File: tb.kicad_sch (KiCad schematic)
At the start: 67 parts, among them U4 JHL6340SLLSQ, U5 MX25L8006EM1I-12G, U6 SI52112-B6-GT, U7 MX25L8006EM2I-12G, Y1 ABM8G-25.000MHZ-B4Y-T, Y2 ABM8G-25.000MHZ-B4Y-T

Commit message: Run kmake loclib
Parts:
- C100, C102, C103, C105, C106, C107, C108, C109, C110, C111, C112, C99: footprint antmicro-footprints:C_0402_1005Metric -> thunderbolt-adapter-footprints:C_0402_1005Metric; symbol antmicroCapacitors0402:C_220n_0402 -> thunderbolt-adapter:C_220n_0402
- C101, C104, C115, C98: footprint antmicro-footprints:C_0402_1005Metric -> thunderbolt-adapter-footprints:C_0402_1005Metric; symbol antmicroCapacitors0402:C_100n_0402 -> thunderbolt-adapter:C_100n_0402
- C113, C114, C116, C117: footprint antmicro-footprints:C_0402_1005Metric -> thunderbolt-adapter-footprints:C_0402_1005Metric; symbol antmicroCapacitors0402:C_10p_0402 -> thunderbolt-adapter:C_10p_0402
- R50, R51, R52, R53: footprint antmicro-footprints:R_0402_1005Metric -> thunderbolt-adapter-footprints:R_0402_1005Metric; symbol antmicroResistors0402:R_3k3_0402 -> thunderbolt-adapter:R_3k3_0402
- R54, R55, R70, R71, R82: footprint antmicro-footprints:R_0402_1005Metric -> thunderbolt-adapter-footprints:R_0402_1005Metric; symbol antmicroResistors0402:R_1M_0402 -> thunderbolt-adapter:R_1M_0402
- R56, R64, R65, R66, R67, R78, R79, R80, R83, R85: footprint antmicro-footprints:R_0402_1005Metric -> thunderbolt-adapter-footprints:R_0402_1005Metric; symbol antmicroResistors0402:R_10k_0402 -> thunderbolt-adapter:R_10k_0402
- R57, R60, R72, R75, R77, R81, R84, R86, R87, R90: footprint antmicro-footprints:R_0402_1005Metric -> thunderbolt-adapter-footprints:R_0402_1005Metric; symbol antmicroResistors0402:R_100k_0402 -> thunderbolt-adapter:R_100k_0402
- R58, R59, R61, R62: footprint antmicro-footprints:R_0402_1005Metric -> thunderbolt-adapter-footprints:R_0402_1005Metric; symbol antmicroResistors0402:R_2k2_0402 -> thunderbolt-adapter:R_2k2_0402
- R63, R76: footprint antmicro-footprints:R_0402_1005Metric -> thunderbolt-adapter-footprints:R_0402_1005Metric; symbol antmicroResistors0402:R_14k_0402 -> thunderbolt-adapter:R_14k_0402
- R68, R73: footprint antmicro-footprints:R_0402_1005Metric -> thunderbolt-adapter-footprints:R_0402_1005Metric; symbol antmicroResistors0402:R_499R_0402 -> thunderbolt-adapter:R_499R_0402
- R69: footprint antmicro-footprints:R_0402_1005Metric -> thunderbolt-adapter-footprints:R_0402_1005Metric; symbol antmicroResistors0402:R_4k75_0.5%_0402 -> thunderbolt-adapter:R_4k75_0.5%_0402
- R74: footprint antmicro-footprints:R_0402_1005Metric -> thunderbolt-adapter-footprints:R_0402_1005Metric; symbol antmicroResistors0402:R_3k01_0402 -> thunderbolt-adapter:R_3k01_0402
- R88, R89: footprint antmicro-footprints:R_0402_1005Metric -> thunderbolt-adapter-footprints:R_0402_1005Metric; symbol antmicroResistors0402:R_100R_0402 -> thunderbolt-adapter:R_100R_0402
- U4: footprint antmicro-footprints:JHL6340SLLSQ -> thunderbolt-adapter-footprints:JHL6340SLLSQ; symbol antmicroInterfaceControllers:JHL6340SLLSQ -> thunderbolt-adapter:JHL6340SLLSQ
- U5: footprint antmicro-footprints:SOIC-8_3.9x4.9x1.75mm_P1.27mm -> thunderbolt-adapter-footprints:SOIC-8_3.9x4.9x1.75mm_P1.27mm; symbol antmicroMemory:MX25L8006EM1I-12G -> thunderbolt-adapter:MX25L8006EM1I-12G
- U6: footprint antmicro-footprints:TSSOP-8_3x4.4mm_P0.65mm -> thunderbolt-adapter-footprints:TSSOP-8_3x4.4mm_P0.65mm; symbol antmicroClockTimingClockGeneratorsPLLsFrequencySynthesizers:SI52112-B6-GT -> thunderbolt-adapter:SI52112-B6-GT
- U7: footprint antmicro-footprints:SOIC-8_5.3x5.3x2mm_P1.27mm -> thunderbolt-adapter-footprints:SOIC-8_5.3x5.3x2mm_P1.27mm; symbol antmicroMemory:MX25L8006EM2I-12G -> thunderbolt-adapter:MX25L8006EM2I-12G
- Y1, Y2: footprint antmicro-footprints:Oscillator_SMD_Geyer_KX-7-4Pin_3.2x2.5mm -> thunderbolt-adapter-footprints:Oscillator_SMD_Geyer_KX-7-4Pin_3.2x2.5mm; symbol antmicroCrystals:ABM8G-25.000MHZ-B4Y-T -> thunderbolt-adapter:ABM8G-25.000MHZ-B4Y-T

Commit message: Rename project to thunderbolt-gpu-adapter
Fix Amphenol 10146070-113Y0LF footprint
Add missing 3D models, update selected footprints
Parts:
- C100, C102, C103, C105, C106, C107, C108, C109, C110, C111, C112, C99: footprint thunderbolt-adapter-footprints:C_0402_1005Metric -> thunderbolt-gpu-adapter-footprints:C_0402_1005Metric; symbol thunderbolt-adapter:C_220n_0402 -> thunderbolt-gpu-adapter:C_220n_0402
- C101, C104, C115, C98: footprint thunderbolt-adapter-footprints:C_0402_1005Metric -> thunderbolt-gpu-adapter-footprints:C_0402_1005Metric; symbol thunderbolt-adapter:C_100n_0402 -> thunderbolt-gpu-adapter:C_100n_0402
- C113, C114, C116, C117: footprint thunderbolt-adapter-footprints:C_0402_1005Metric -> thunderbolt-gpu-adapter-footprints:C_0402_1005Metric; symbol thunderbolt-adapter:C_10p_0402 -> thunderbolt-gpu-adapter:C_10p_0402
- R50, R51, R52, R53: footprint thunderbolt-adapter-footprints:R_0402_1005Metric -> thunderbolt-gpu-adapter-footprints:R_0402_1005Metric; symbol thunderbolt-adapter:R_3k3_0402 -> thunderbolt-gpu-adapter:R_3k3_0402
- R54, R55, R70, R71, R82: footprint thunderbolt-adapter-footprints:R_0402_1005Metric -> thunderbolt-gpu-adapter-footprints:R_0402_1005Metric; symbol thunderbolt-adapter:R_1M_0402 -> thunderbolt-gpu-adapter:R_1M_0402
- R56, R64, R65, R66, R67, R78, R79, R80, R83, R85: footprint thunderbolt-adapter-footprints:R_0402_1005Metric -> thunderbolt-gpu-adapter-footprints:R_0402_1005Metric; symbol thunderbolt-adapter:R_10k_0402 -> thunderbolt-gpu-adapter:R_10k_0402
- R57, R60, R72, R75, R77, R81, R84, R86, R87, R90: footprint thunderbolt-adapter-footprints:R_0402_1005Metric -> thunderbolt-gpu-adapter-footprints:R_0402_1005Metric; symbol thunderbolt-adapter:R_100k_0402 -> thunderbolt-gpu-adapter:R_100k_0402
- R58, R59, R61, R62: footprint thunderbolt-adapter-footprints:R_0402_1005Metric -> thunderbolt-gpu-adapter-footprints:R_0402_1005Metric; symbol thunderbolt-adapter:R_2k2_0402 -> thunderbolt-gpu-adapter:R_2k2_0402
- R63, R76: footprint thunderbolt-adapter-footprints:R_0402_1005Metric -> thunderbolt-gpu-adapter-footprints:R_0402_1005Metric; symbol thunderbolt-adapter:R_14k_0402 -> thunderbolt-gpu-adapter:R_14k_0402
- R68, R73: footprint thunderbolt-adapter-footprints:R_0402_1005Metric -> thunderbolt-gpu-adapter-footprints:R_0402_1005Metric; symbol thunderbolt-adapter:R_499R_0402 -> thunderbolt-gpu-adapter:R_499R_0402
- R69: footprint thunderbolt-adapter-footprints:R_0402_1005Metric -> thunderbolt-gpu-adapter-footprints:R_0402_1005Metric; symbol thunderbolt-adapter:R_4k75_0.5%_0402 -> thunderbolt-gpu-adapter:R_4k75_0.5%_0402
- R74: footprint thunderbolt-adapter-footprints:R_0402_1005Metric -> thunderbolt-gpu-adapter-footprints:R_0402_1005Metric; symbol thunderbolt-adapter:R_3k01_0402 -> thunderbolt-gpu-adapter:R_3k01_0402
- R88, R89: footprint thunderbolt-adapter-footprints:R_0402_1005Metric -> thunderbolt-gpu-adapter-footprints:R_0402_1005Metric; symbol thunderbolt-adapter:R_100R_0402 -> thunderbolt-gpu-adapter:R_100R_0402
- U4: footprint thunderbolt-adapter-footprints:JHL6340SLLSQ -> thunderbolt-gpu-adapter-footprints:JHL6340SLLSQ; symbol thunderbolt-adapter:JHL6340SLLSQ -> thunderbolt-gpu-adapter:JHL6340SLLSQ
- U5: footprint thunderbolt-adapter-footprints:SOIC-8_3.9x4.9x1.75mm_P1.27mm -> thunderbolt-gpu-adapter-footprints:SOIC-8_3.9x4.9x1.75mm_P1.27mm; symbol thunderbolt-adapter:MX25L8006EM1I-12G -> thunderbolt-gpu-adapter:MX25L8006EM1I-12G
- U6: footprint thunderbolt-adapter-footprints:TSSOP-8_3x4.4mm_P0.65mm -> thunderbolt-gpu-adapter-footprints:TSSOP-8_3x4.4mm_P0.65mm; symbol thunderbolt-adapter:SI52112-B6-GT -> thunderbolt-gpu-adapter:SI52112-B6-GT
- U7: footprint thunderbolt-adapter-footprints:SOIC-8_5.3x5.3x2mm_P1.27mm -> thunderbolt-gpu-adapter-footprints:SOIC-8_5.3x5.3x2mm_P1.27mm; symbol thunderbolt-adapter:MX25L8006EM2I-12G -> thunderbolt-gpu-adapter:MX25L8006EM2I-12G
- Y1, Y2: footprint thunderbolt-adapter-footprints:Oscillator_SMD_Geyer_KX-7-4Pin_3.2x2.5mm -> thunderbolt-gpu-adapter-footprints:Oscillator_SMD_Geyer_KX-7-4Pin_3.2x2.5mm; symbol thunderbolt-adapter:ABM8G-25.000MHZ-B4Y-T -> thunderbolt-gpu-adapter:ABM8G-25.000MHZ-B4Y-T

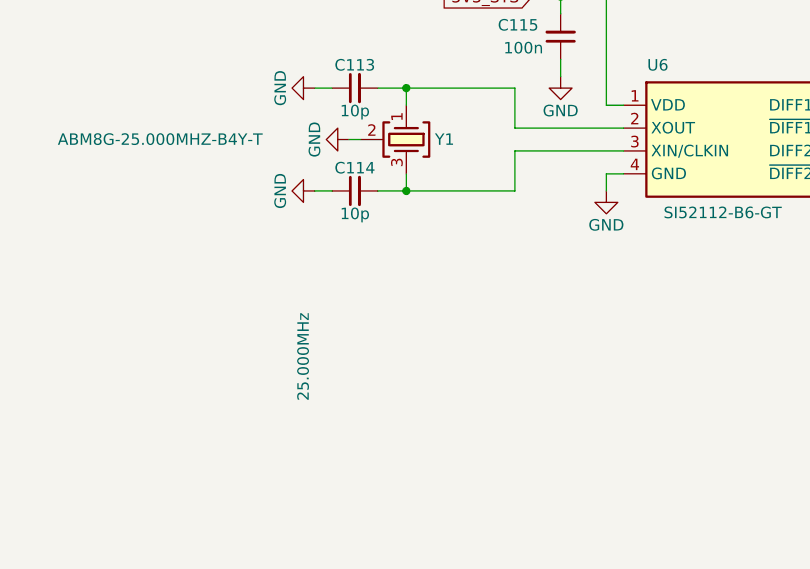
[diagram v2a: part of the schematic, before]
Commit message: Fix PCIe power switch - layout, bump revision to 1.1.2
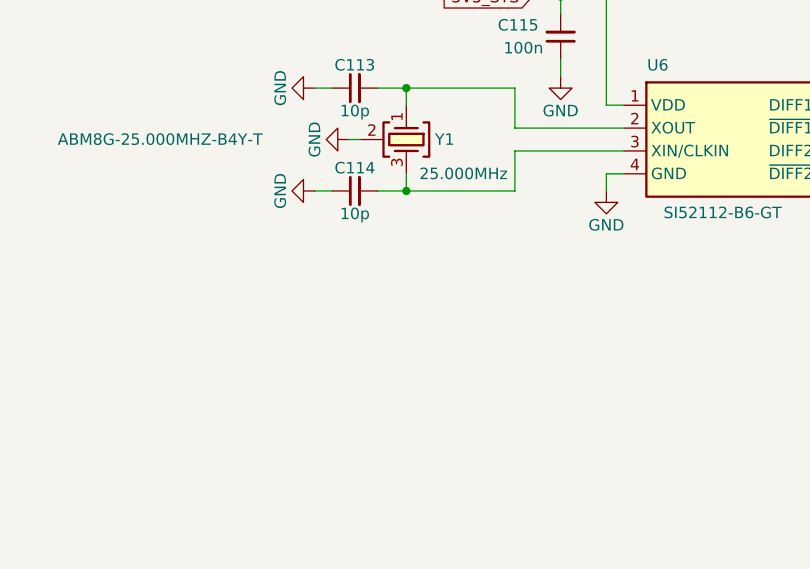
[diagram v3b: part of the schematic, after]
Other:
- company: (none) -> Antmicro Ltd
- title: Thunderbolt to PCIe bridge -> Thunderbolt GPU Adapter
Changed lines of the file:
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@@
   (paper "A3" portrait)
   (title_block
-    (title "Thunderbolt to PCIe bridge")
-    (date "2023-05-09")
-    (rev "1.1.1")
+    (title "Thunderbolt GPU Adapter")
+    (date "2023-11-21")
+    (rev "1.1.2")
+    (company "Antmicro Ltd")
     (comment 1 "www.antmicro.com")
-    (comment 2 "Antmicro Ltd.")
   )
   (junction (at 219.71 208.28) (diameter 0) (color 0 0 0 0)
@@
       (effects (font (size 1.27 1.27) (thickness 0.15)) (justify left bottom) hide)
     )
-    (property "Val" "25.000MHz" (id 9) (at 186.69 386.08 0))
-    (pin "1")
-    (pin "2")
+    (property "Val" "25.000MHz" (id 9) (at 204.47 365.76 90))
+    (pin "1")
+    (pin "2")

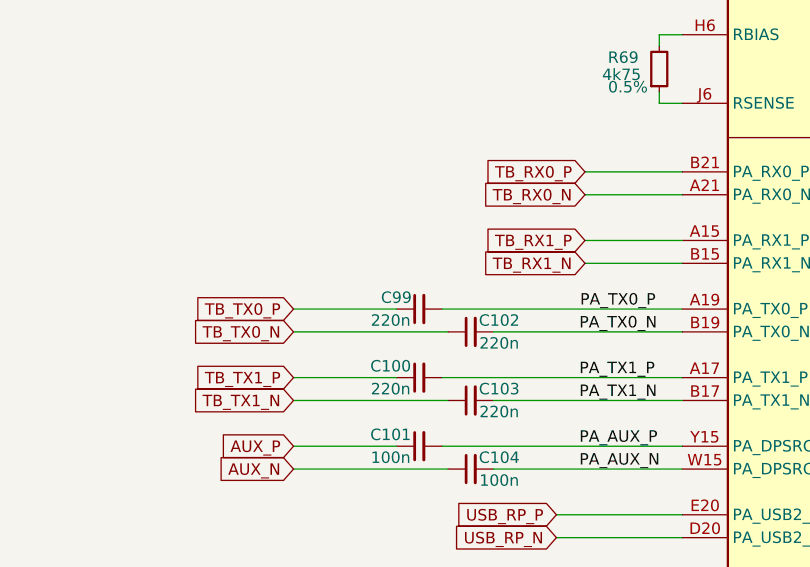
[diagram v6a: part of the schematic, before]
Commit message: Fix ERC errors on schematic:
	- Fix first batch of GND ERC
	- Fix second batch of GND ERC
	- Fix ERC of 0R_0603
	- Fix erc BC817-25W
	- Fix erc 220n_0402
	- Fix erc PCIe_x16_10146070-113Y0LF-vertical
	- Fix erc 100n_0402
	- Fix erc 10u_0805_35V
	- Correct BC817-25W_1
	- Correct erc R_98R_0402_1
	- Correct 10K_0402
	- Correct 22u/16V
	- Correct 100k
	- Correct 499R
	- Correct 3k01
	- Correct 10p
	- Correct 330R
	- Correct 3k3
	- Correct 1n4148WS-7-F
	- Correct SI7613DN-T1GE3_1 and TP's
	- Correct LED_G_0603_KP-1608CGCK_1
	- Correct 2k2_0402
	- Correct DZDH0401DW_1
	- Correct 22u_0603
	- Correct TP 0.75mm
	- Correct 0R_0402
	- Correct 0R_22.4A
	- Correct Batch of Resitors
	- Correct Batch of Capacitors
	- Correct USB PD controller
	- Correct batch of pasives
	- Correct MM3Z3V3C
	- Correct LM1117MP-3.3_NOPB
	- Correct Flash memory
	- Correct MP2386GG_1_1
	- Fix symbol LT8350RV#PBF and correct it on schematic
	- Add pwr flags
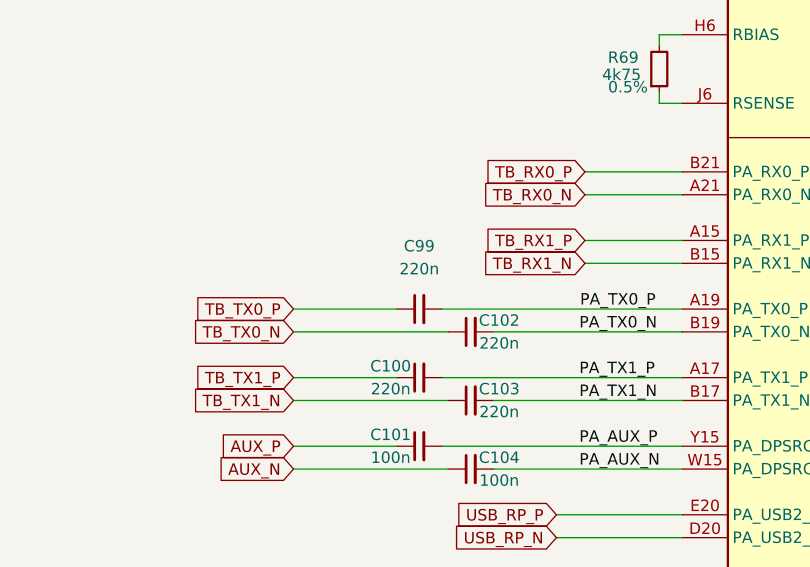
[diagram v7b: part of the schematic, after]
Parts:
- C100, C102, C103, C105, C106, C107, C108, C109, C110, C111, C112, C99: Manufacturer Yaego -> YAGEO
- U6: Manufacturer Skyworks -> Skyworks Solutions
